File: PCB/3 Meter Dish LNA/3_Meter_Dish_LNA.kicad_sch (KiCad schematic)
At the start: 24 parts, among them J1 Conn_Coaxial, J2 Conn_Coaxial, J3 Conn_Coaxial, U1 PMA2-63LN+, U2 PMA2-63LN+, U3 YAT-1A+, U4 L7805, U5 L7805

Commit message: Footprints assigned, ERC pass
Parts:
- C1, C10, C11, C12, C2, C3, C4, C5, C6, C7, C8, C9: footprint (none) -> Capacitor_SMD:C_0402_1005Metric
- J1, J2, J3: footprint (none) -> Connector_Coaxial:SMA_Molex_73251-1153_EdgeMount_Horizontal
- L1, L2: footprint (none) -> Inductor_SMD:L_0402_1005Metric
- R1, R2: footprint (none) -> Resistor_SMD:R_0402_1005Metric
- U1, U2: footprint SON8_PMA2_MNC -> Imports:SON8_PMA2_MNC
- U3: footprint MC1630_MNC -> Imports:MC1630_MNC
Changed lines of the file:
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@@
       (effects (font (size 1.27 1.27)) (justify left))
     )
-    (property "Footprint" "" (at 243.84 110.49 0)
+    (property "Footprint" "Capacitor_SMD:C_0402_1005Metric" (at 243.84 110.49 0)
       (effects (font (size 1.27 1.27)) hide)
     )
@@
       (effects (font (size 1.27 1.27)))
     )
-    (property "Footprint" "" (at 50.8 148.59 0)
+    (property "Footprint" "Capacitor_SMD:C_0402_1005Metric" (at 50.8 148.59 0)
       (effects (font (size 1.27 1.27)) hide)
     )
@@
       (effects (font (size 1.27 1.27)))
     )
-    (property "Footprint" "" (at 123.19 151.13 0)
+    (property "Footprint" "Capacitor_SMD:C_0402_1005Metric" (at 123.19 151.13 0)
       (effects (font (size 1.27 1.27)) hide)
     )
@@
       (effects (font (size 1.27 1.27)))
     )
-    (property "Footprint" "" (at 50.8 57.15 0)
+    (property "Footprint" "Capacitor_SMD:C_0402_1005Metric" (at 50.8 57.15 0)
       (effects (font (size 1.27 1.27)) hide)
     )
@@
       (effects (font (size 1.27 1.27)) (justify left))
     )
-    (property "Footprint" "" (at 218.44 43.18 0)
+    (property "Footprint" "Connector_Coaxial:SMA_Molex_73251-1153_EdgeMount_Horizontal" (at 218.44 43.18 0)
       (effects (font (size 1.27 1.27)) hide)
     )
@@
       (effects (font (size 1.27 1.27)))
     )
-    (property "Footprint" "" (at 123.19 135.89 0)
+    (property "Footprint" "Capacitor_SMD:C_0402_1005Metric" (at 123.19 135.89 0)
       (effects (font (size 1.27 1.27)) hide)
     )
@@
       (effects (font (size 1.27 1.27)) (justify left))
     )
-    (property "Footprint" "" (at 201.93 110.49 0)
+    (property "Footprint" "Capacitor_SMD:C_0402_1005Metric" (at 201.93 110.49 0)
       (effects (font (size 1.27 1.27)) hide)
     )
@@
       (effects (font (size 1.27 1.27)) (justify left))
     )
-    (property "Footprint" "" (at 114.3 52.07 0)
+    (property "Footprint" "Inductor_SMD:L_0402_1005Metric" (at 114.3 52.07 0)
       (effects (font (size 1.27 1.27)) hide)
     )
@@
       (effects (font (size 1.524 1.524)))
     )
-    (property "Footprint" "SON8_PMA2_MNC" (at 57.15 52.07 0)
+    (property "Footprint" "Imports:SON8_PMA2_MNC" (at 57.15 52.07 0)
       (effects (font (size 1.27 1.27) italic) hide)
     )
@@
       (effects (font (size 1.27 1.27)) (justify left))
     )
-    (property "Footprint" "" (at 52.832 137.16 90)
+    (property "Footprint" "Resistor_SMD:R_0402_1005Metric" (at 52.832 137.16 90)
       (effects (font (size 1.27 1.27)) hide)
     )
@@
       (effects (font (size 1.27 1.27)) (justify left))
     )
-    (property "Footprint" "" (at 243.84 81.28 0)
+    (property "Footprint" "Capacitor_SMD:C_0402_1005Metric" (at 243.84 81.28 0)
       (effects (font (size 1.27 1.27)) hide)
     )
@@
       (effects (font (size 1.27 1.27)) (justify left))
     )
-    (property "Footprint" "" (at 201.93 81.28 0)
+    (property "Footprint" "Capacitor_SMD:C_0402_1005Metric" (at 201.93 81.28 0)
       (effects (font (size 1.27 1.27)) hide)
     )
@@
       (effects (font (size 1.524 1.524)))
     )
-    (property "Footprint" "MC1630_MNC" (at 57.15 95.25 0)
+    (property "Footprint" "Imports:MC1630_MNC" (at 57.15 95.25 0)
       (effects (font (size 1.27 1.27) italic) hide)
     )
@@
       (effects (font (size 1.27 1.27)))
     )
-    (property "Footprint" "" (at 123.19 30.48 0)
+    (property "Footprint" "Capacitor_SMD:C_0402_1005Metric" (at 123.19 30.48 0)
       (effects (font (size 1.27 1.27)) hide)
     )
@@
       (effects (font (size 1.27 1.27)))
     )
-    (property "Footprint" "" (at 39.37 57.15 0)
+    (property "Footprint" "Connector_Coaxial:SMA_Molex_73251-1153_EdgeMount_Horizontal" (at 39.37 57.15 0)
       (effects (font (size 1.27 1.27)) hide)
     )
@@
       (effects (font (size 1.27 1.27)))
     )
-    (property "Footprint" "" (at 134.62 151.13 0)
+    (property "Footprint" "Connector_Coaxial:SMA_Molex_73251-1153_EdgeMount_Horizontal" (at 134.62 151.13 0)
       (effects (font (size 1.27 1.27)) hide)
     )
@@
       (effects (font (size 1.27 1.27)))
     )
-    (property "Footprint" "" (at 123.19 121.92 0)
+    (property "Footprint" "Capacitor_SMD:C_0402_1005Metric" (at 123.19 121.92 0)
       (effects (font (size 1.27 1.27)) hide)
     )
@@
       (effects (font (size 1.27 1.27)))
     )
-    (property "Footprint" "" (at 123.19 44.45 0)
+    (property "Footprint" "Capacitor_SMD:C_0402_1005Metric" (at 123.19 44.45 0)
       (effects (font (size 1.27 1.27)) hide)
     )
@@
       (effects (font (size 1.27 1.27)) (justify left))
     )
-    (property "Footprint" "" (at 114.3 143.51 0)
+    (property "Footprint" "Inductor_SMD:L_0402_1005Metric" (at 114.3 143.51 0)
       (effects (font (size 1.27 1.27)) hide)
     )
@@
       (effects (font (size 1.27 1.27)))
     )
-    (property "Footprint" "" (at 123.19 59.69 0)
+    (property "Footprint" "Capacitor_SMD:C_0402_1005Metric" (at 123.19 59.69 0)
       (effects (font (size 1.27 1.27)) hide)
     )
@@
       (effects (font (size 1.27 1.27)) (justify left))
     )
-    (property "Footprint" "" (at 52.832 45.72 90)
+    (property "Footprint" "Resistor_SMD:R_0402_1005Metric" (at 52.832 45.72 90)
       (effects (font (size 1.27 1.27)) hide)
     )
@@
       (effects (font (size 1.524 1.524)))
     )
-    (property "Footprint" "SON8_PMA2_MNC" (at 57.15 143.51 0)
+    (property "Footprint" "Imports:SON8_PMA2_MNC" (at 57.15 143.51 0)
       (effects (font (size 1.27 1.27) italic) hide)
     )

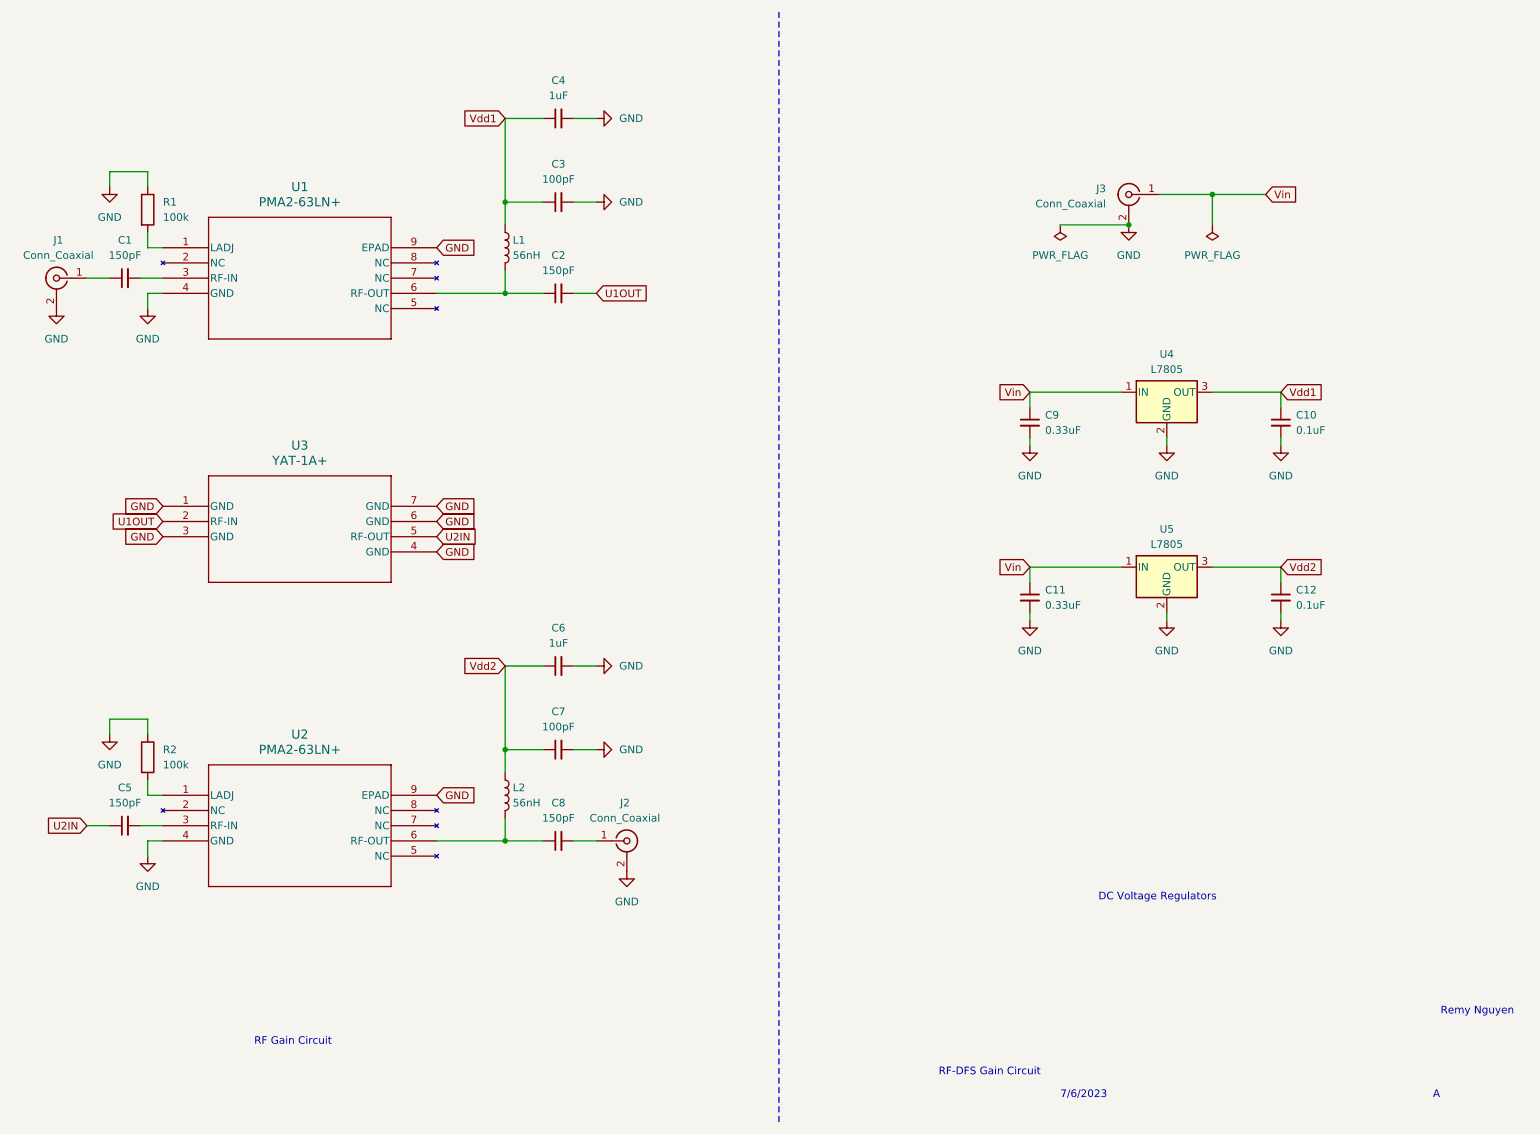
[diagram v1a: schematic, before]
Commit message: PCB Rev A Complete, DRC Pass
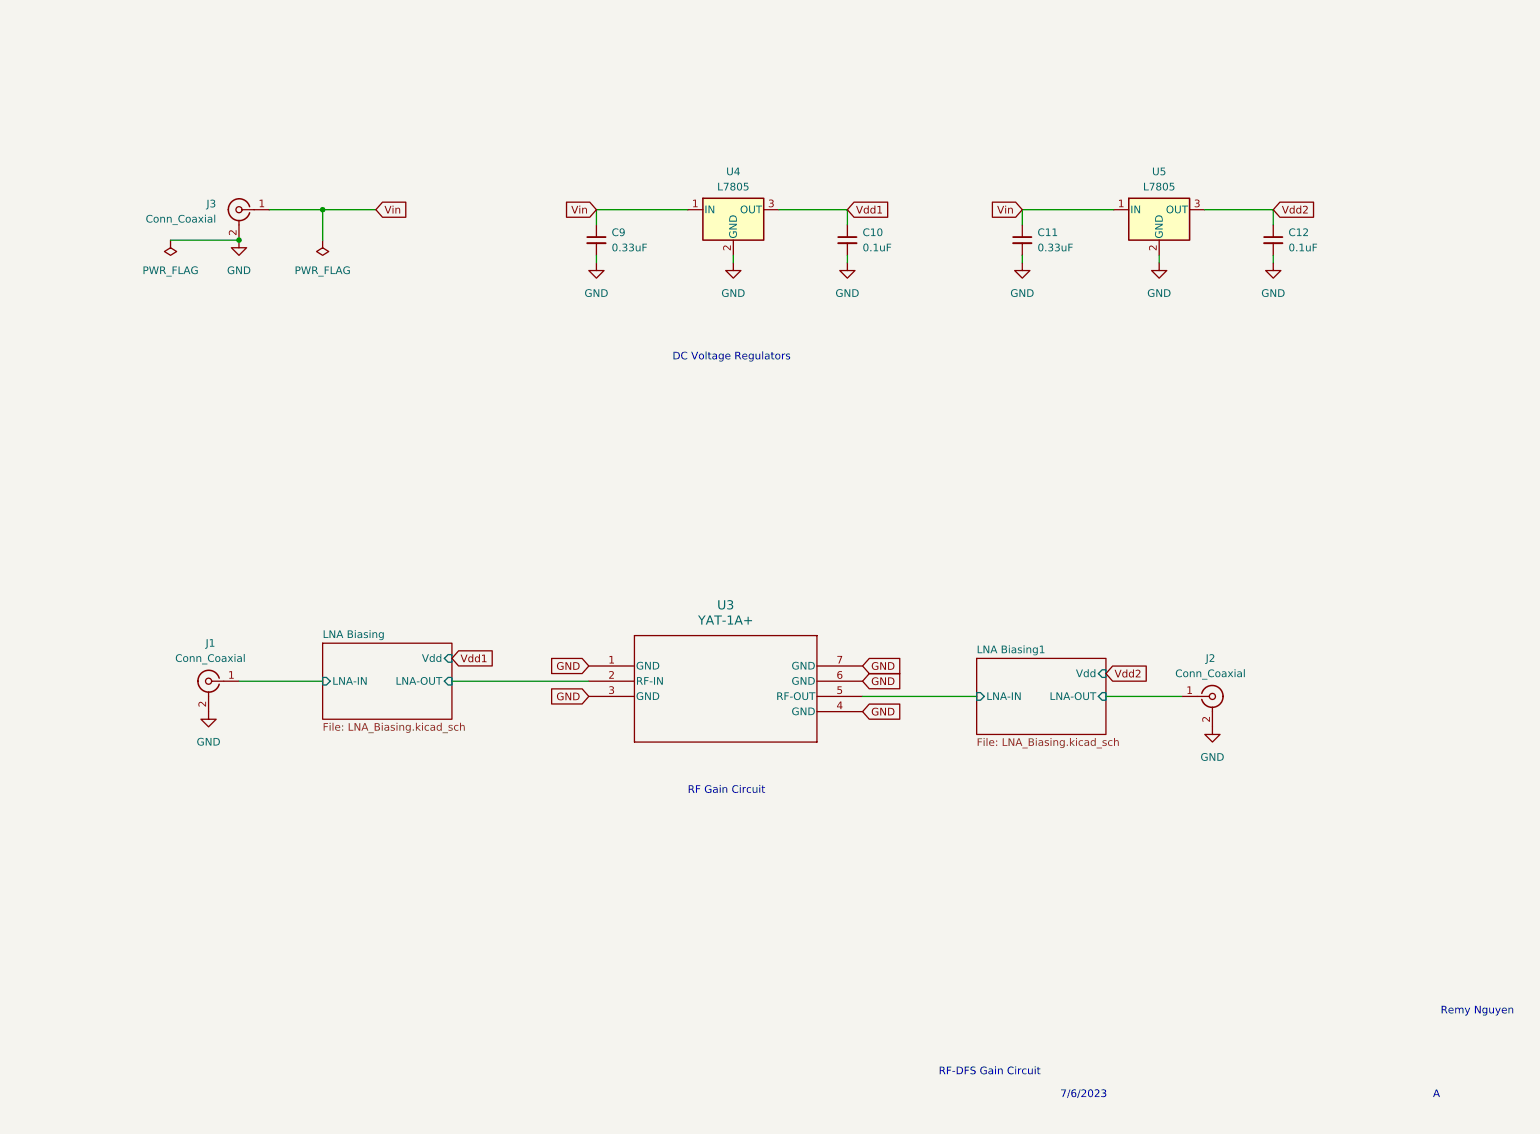
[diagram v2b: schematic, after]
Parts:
- removed C1, C2, C5, C8: 150pF, Capacitor_SMD:C_0402_1005Metric, symbol Device:C_Small
- removed C3, C7: 100pF, Capacitor_SMD:C_0402_1005Metric, symbol Device:C_Small
- removed C4, C6: 1uF, Capacitor_SMD:C_0402_1005Metric, symbol Device:C_Small
- removed L1, L2: 56nH, Inductor_SMD:L_0402_1005Metric, symbol Device:L
- removed R1, R2: 100k, Resistor_SMD:R_0402_1005Metric, symbol Device:R
- removed U1, U2: PMA2-63LN+, Imports:SON8_PMA2_MNC, symbol PMA2-63LN+:PMA2-63LN+
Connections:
- net LNA Biasing1/LNA-OUT: now reaches J2.1 (In)
- net LNA Biasing/LNA-IN: now reaches J1.1 (In)
- net U1OUT renamed LNA Biasing/LNA-OUT
- net U2IN renamed LNA Biasing1/LNA-IN
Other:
- added sheet LNA Biasing (LNA_Biasing.kicad_sch)
- added sheet LNA Biasing1 (LNA_Biasing.kicad_sch)
- moved on the sheet: C10, C11, C12, C9, J1, J3, U3, U4, U5
